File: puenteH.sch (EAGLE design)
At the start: 20 parts, among them IC1 LM393N, Q1 IRF4905, Q2 IRLZ44Z, Q3 IRLZ44Z, Q4 IRF4905, Q5 IRF540, Q6 IRF540, Q7 IRF9530, Q8 IRF9530

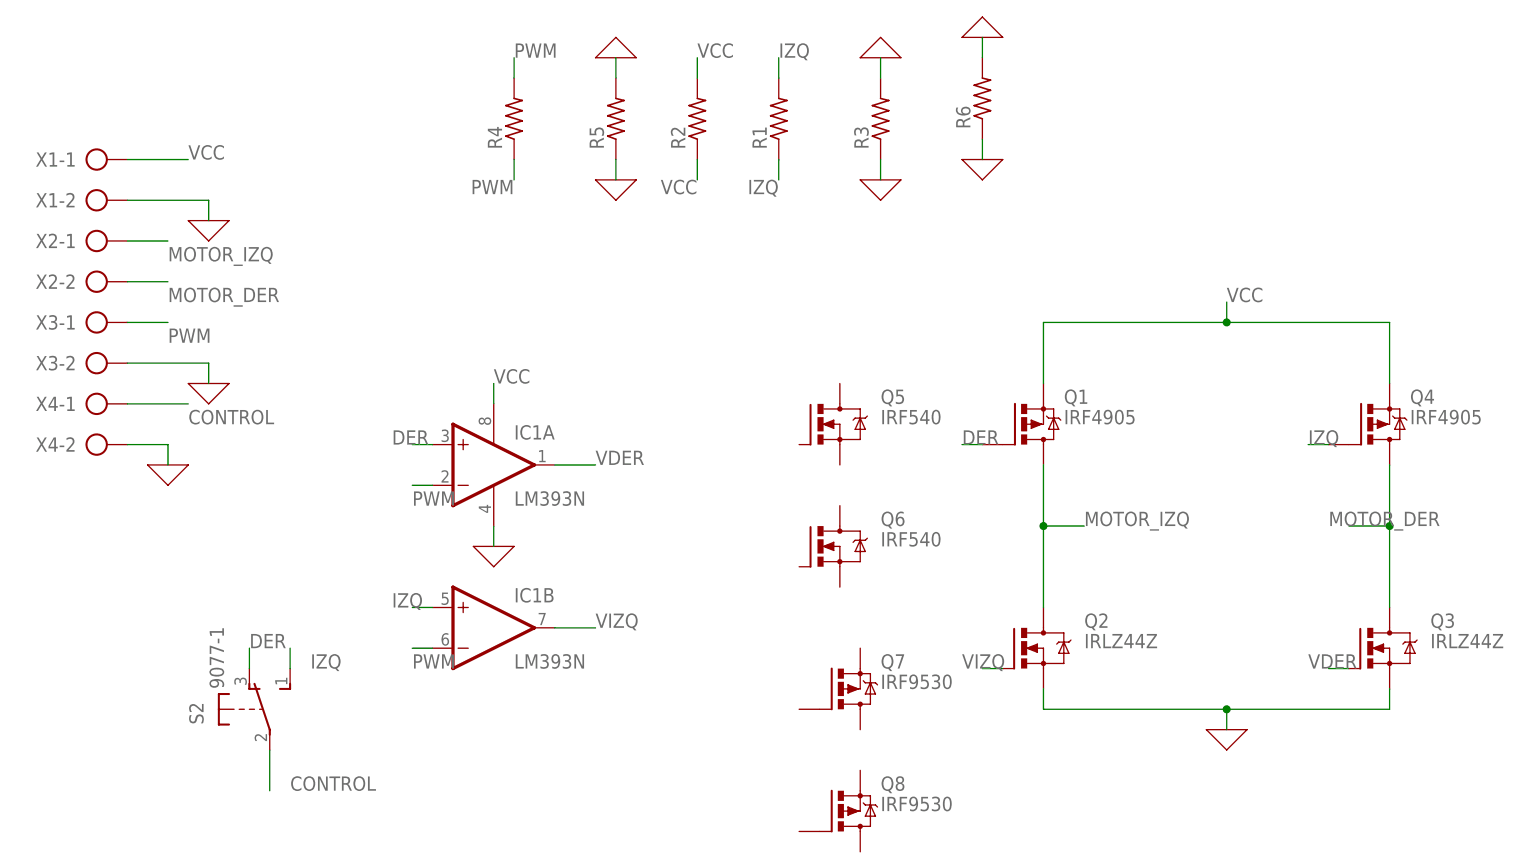
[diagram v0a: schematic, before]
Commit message: Ready to get gerbers, a little optimized, not using 'compontents that are really going to be used' but it is good enough
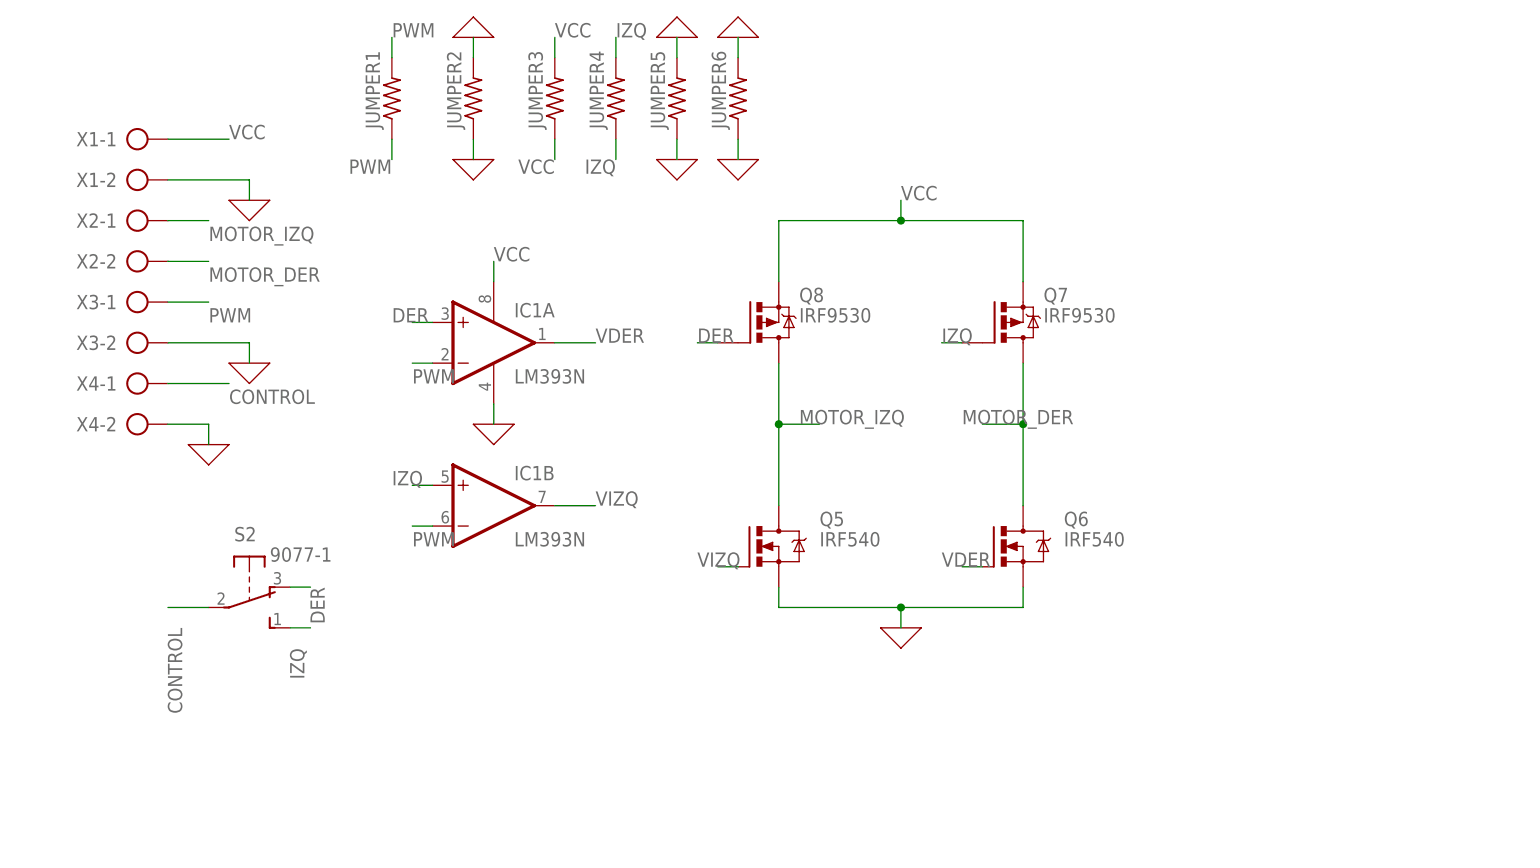
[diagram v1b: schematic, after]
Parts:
- removed Q1, Q4: IRF4905, transistor-power:IRF4905
- removed Q2, Q3: IRLZ44Z, transistor-power:IRLZ44Z
- removed R1, R5: (no value), rcl:R-US_0204/7
- removed R2, R3, R4, R6: (no value), rcl:R-US_0204/5
- added JUMPER1, JUMPER3, JUMPER4, JUMPER5, JUMPER6: (no value), rcl:R-US_0204/5
- added JUMPER2: (no value), rcl:R-US_0204/7
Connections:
- net 0: now also JUMPER2.1, JUMPER2.2, JUMPER5.1, JUMPER5.2, JUMPER6.1, JUMPER6.2, Q5.S, Q6.S; no longer Q2.S, Q3.S, R3.1, R3.2, R5.1, R5.2, R6.1, R6.2
- net DER: now also Q8.G; no longer Q1.G
- net IZQ: now also JUMPER4.1, JUMPER4.2, Q7.G; no longer Q4.G, R1.1, R1.2
- net MOTOR_DER: now also Q6.D, Q7.D; no longer Q3.D, Q4.D
- net MOTOR_IZQ: now also Q5.D, Q8.D; no longer Q1.D, Q2.D
- net PWM: now also JUMPER1.1, JUMPER1.2; no longer R4.1, R4.2
- net VCC: now also JUMPER3.1, JUMPER3.2, Q7.S, Q8.S; no longer Q1.S, Q4.S, R2.1, R2.2
- net VDER: now also Q6.G; no longer Q3.G
- net VIZQ: now also Q5.G; no longer Q2.G
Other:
- moved on the sheet: IC1A, IC1B, Q5, Q6, Q7, Q8, S2, X1-1, X1-2, X2-1, X2-2, X3-1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
